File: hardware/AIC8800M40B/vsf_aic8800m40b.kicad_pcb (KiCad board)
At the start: 4 copper layers, 36.8 x 57.2 mm, 86 parts, among them J1 USB_A, J2 USB_C_Receptacle_USB2.0, J3 USB_C_Receptacle_USB2.0, J4 Micro_SD_Card_Det1, J6 Conn_Coaxial, J7 Conn_Coaxial, J8 Conn_02x15_Odd_Even, Q1 S9013, SW1 SW_Push, SW2 SW_Push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

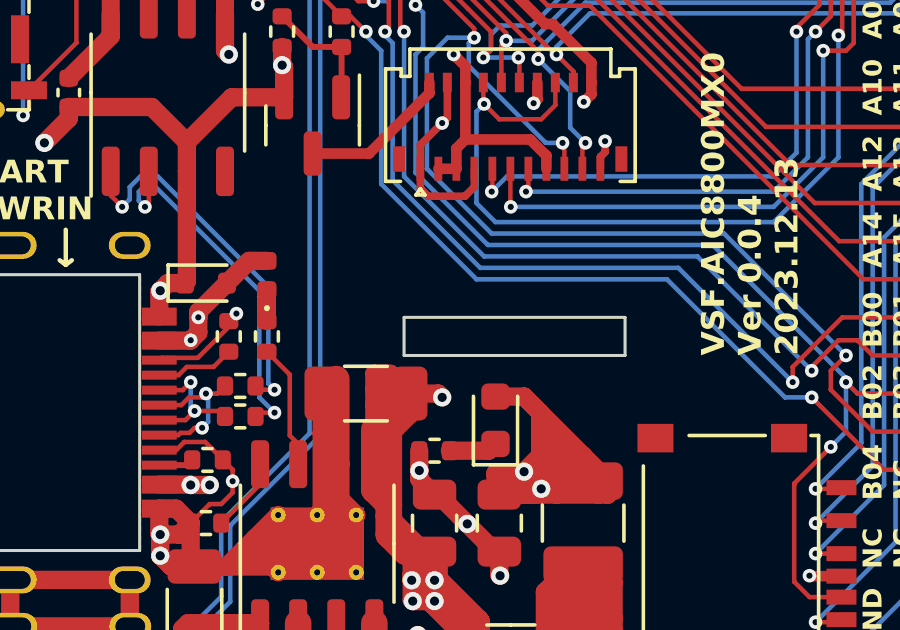
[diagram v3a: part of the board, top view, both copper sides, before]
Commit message: [hardware/aic8800m40b] update LED footprint to 0603
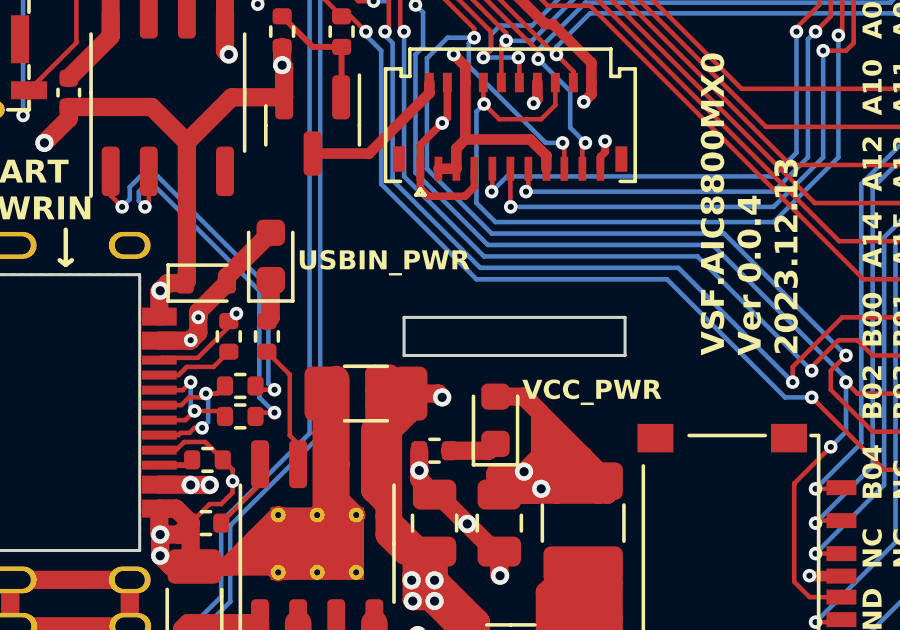
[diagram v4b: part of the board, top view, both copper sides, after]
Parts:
- D2: footprint LED_SMD:LED_0402_1005Metric -> LED_SMD:LED_0603_1608Metric
- moved D2 0.65 mm to (213.5, 124.3)
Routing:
- net /USB5V_IN: track 61.6 -> 62.2 mm
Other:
- board text added: "USBIN_PWR"
- board text added: "VCC_PWR"
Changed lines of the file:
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@@
     )
   )
-  (footprint "LED_SMD:LED_0402_1005Metric" (layer "F.Cu")
-    (at 213.36 124.968 90)
-    (descr "LED SMD 0402 (1005 Metric), square (rectangular) end terminal, IPC_7351 nominal, (Body size source: http://www.tortai-tech.com/upload/download/2011102023233369053.pdf), generated with kicad-footprint-generator")
+  (footprint "LED_SMD:LED_0603_1608Metric" (layer "F.Cu")
+    (at 213.487 124.333 90)
+    (descr "LED SMD 0603 (1608 Metric), square (rectangular) end terminal, IPC_7351 nominal, (Body size source: http://www.tortai-tech.com/upload/download/2011102023233369053.pdf), generated with kicad-footprint-generator")
     (tags "LED")
     (property "Sheetfile" "vsf_aic8800m40b.kicad_sch")
@@
     (property "ki_keywords" "LED diode")
     (attr smd)
-    (fp_text reference "D2" (at 1.524 0 180) (layer "F.SilkS") hide
-        (effects (font (size 0.762 0.762) (thickness 0.1524) bold))
+    (fp_text reference "D2" (at 0 -1.43 90) (layer "F.SilkS") hide
+        (effects (font (size 1 1) (thickness 0.15)))
     )
-    (fp_text value "LED, RED" (at 0 1.17 90) (layer "F.Fab")
+    (fp_text value "LED, RED" (at 0 1.43 90) (layer "F.Fab")
         (effects (font (size 1 1) (thickness 0.15)))
     )
     (fp_text user "${REFERENCE}" (at 0 0 90) (layer "F.Fab")
-        (effects (font (size 0.25 0.25) (thickness 0.04)))
+        (effects (font (size 0.4 0.4) (thickness 0.06)))
     )
-    (fp_circle (center -1.09 0) (end -1.04 0)
-      (stroke (width 0.1) (type solid)) (fill none) (layer "F.SilkS"))
-    (fp_line (start -0.93 -0.47) (end 0.93 -0.47)
+    (fp_line (start -1.485 -0.735) (end -1.485 0.735)
+      (stroke (width 0.12) (type solid)) (layer "F.SilkS"))
+    (fp_line (start -1.485 0.735) (end 0.8 0.735)
+      (stroke (width 0.12) (type solid)) (layer "F.SilkS"))
+    (fp_line (start 0.8 -0.735) (end -1.485 -0.735)
+      (stroke (width 0.12) (type solid)) (layer "F.SilkS"))
+    (fp_line (start -1.48 -0.73) (end 1.48 -0.73)
       (stroke (width 0.05) (type solid)) (layer "F.CrtYd"))
-    (fp_line (start -0.93 0.47) (end -0.93 -0.47)
+    (fp_line (start -1.48 0.73) (end -1.48 -0.73)
       (stroke (width 0.05) (type solid)) (layer "F.CrtYd"))
-    (fp_line (start 0.93 -0.47) (end 0.93 0.47)
+    (fp_line (start 1.48 -0.73) (end 1.48 0.73)
       (stroke (width 0.05) (type solid)) (layer "F.CrtYd"))
-    (fp_line (start 0.93 0.47) (end -0.93 0.47)
+    (fp_line (start 1.48 0.73) (end -1.48 0.73)
       (stroke (width 0.05) (type solid)) (layer "F.CrtYd"))
-    (fp_line (start -0.5 -0.25) (end 0.5 -0.25)
-      (stroke (width 0.1) (type solid)) (layer "F.Fab"))
-    (fp_line (start -0.5 0.25) (end -0.5 -0.25)
+    (fp_line (start -0.8 -0.1) (end -0.8 0.4)
       (stroke (width 0.1) (type solid)) (layer "F.Fab"))
-    (fp_line (start -0.4 0.25) (end -0.4 -0.25)
+    (fp_line (start -0.8 0.4) (end 0.8 0.4)
       (stroke (width 0.1) (type solid)) (layer "F.Fab"))
-    (fp_line (start -0.3 0.25) (end -0.3 -0.25)
+    (fp_line (start -0.5 -0.4) (end -0.8 -0.1)
       (stroke (width 0.1) (type solid)) (layer "F.Fab"))
-    (fp_line (start 0.5 -0.25) (end 0.5 0.25)
+    (fp_line (start 0.8 -0.4) (end -0.5 -0.4)
       (stroke (width 0.1) (type solid)) (layer "F.Fab"))
-    (fp_line (start 0.5 0.25) (end -0.5 0.25)
+    (fp_line (start 0.8 0.4) (end 0.8 -0.4)
       (stroke (width 0.1) (type solid)) (layer "F.Fab"))
-    (pad "1" smd roundrect (at -0.485 0 90) (size 0.59 0.64) (layers "F.Cu" "F.Paste" "F.Mask") (roundrect_rratio 0.25)
+    (pad "1" smd roundrect (at -0.7875 0 90) (size 0.875 0.95) (layers "F.Cu" "F.Paste" "F.Mask") (roundrect_rratio 0.25)
       (net 25 "Net-(D2-K)") (pinfunction "K") (pintype "passive"))
-    (pad "2" smd roundrect (at 0.485 0 90) (size 0.59 0.64) (layers "F.Cu" "F.Paste" "F.Mask") (roundrect_rratio 0.25)
+    (pad "2" smd roundrect (at 0.7875 0 90) (size 0.875 0.95) (layers "F.Cu" "F.Paste" "F.Mask") (roundrect_rratio 0.25)
       (net 20 "/USB5V_IN") (pinfunction "A") (pintype "passive"))
-    (model "${KICAD6_3DMODEL_DIR}/LED_SMD.3dshapes/LED_0402_1005Metric.wrl"
+    (model "${KICAD6_3DMODEL_DIR}/LED_SMD.3dshapes/LED_0603_1608Metric.wrl"
       (offset (xyz 0 0 0))
       (scale (xyz 1 1 1))
@@
     (effects (font (size 0.762 0.762) (thickness 0.1524) bold) (justify left bottom))
   )
+  (gr_text "VCC_PWR" (at 221.869 129.159) (layer "F.SilkS")
+    (effects (font (size 0.635 0.635) (thickness 0.1524) bold) (justify left bottom))
+  )
   (gr_text "B04\nNC" (at 234.95 132.461 90) (layer "F.SilkS")
     (effects (font (size 0.635 0.635) (thickness 0.1524) bold) (justify left bottom))
@@
     (effects (font (size 0.635 0.635) (thickness 0.1524) bold) (justify left bottom))
   )
+  (gr_text "USBIN_PWR" (at 214.376 124.841) (layer "F.SilkS")
+    (effects (font (size 0.635 0.635) (thickness 0.1524) bold) (justify left bottom))
+  )
   (gr_text "5V0\nPWR" (at 234.95 142.621 90) (layer "F.SilkS")
     (effects (font (size 0.635 0.635) (thickness 0.1524) bold) (justify left bottom))
@@
   (segment (start 213.1314 137.0076) (end 212.344 137.795) (width 0.6096) (layer "F.Cu") (net 20))
   (segment (start 212.344 136.5588) (end 212.0072 136.5588) (width 0.6096) (layer "F.Cu") (net 20))
+  (segment (start 212.028 125.222) (end 212.028 125.0045) (width 0.6096) (layer "F.Cu") (net 20))
   (segment (start 210.82 127.127) (end 211.074 126.873) (width 0.6096) (layer "F.Cu") (net 20))
   (segment (start 210.947 136.8128) (end 211.201 136.5588) (width 0.6096) (layer "F.Cu") (net 20))
@@
   (segment (start 211.074 126.176) (end 212.028 125.222) (width 0.6096) (layer "F.Cu") (net 20))
   (segment (start 210.807 131.94) (end 210.82 131.953) (width 0.6096) (layer "F.Cu") (net 20))
-  (segment (start 212.767 124.483) (end 213.36 124.483) (width 0.6096) (layer "F.Cu") (net 20))
   (segment (start 210.53616 137.20816) (end 210.947 137.619) (width 0.6096) (layer "F.Cu") (net 20))
+  (segment (start 212.028 125.0045) (end 213.487 123.5455) (width 0.6096) (layer "F.Cu") (net 20))
   (segment (start 210.5784 144.64) (end 211.074 145.1356) (width 0.6096) (layer "F.Cu") (net 20))
   (segment (start 210.947 137.619) (end 211.2838 137.619) (width 0.6096) (layer "F.Cu") (net 20))
@@
   (segment (start 213.1314 136.5588) (end 212.9452 136.5588) (width 0.6096) (layer "F.Cu") (net 20))
   (segment (start 211.074 145.288) (end 211.074 145.994703) (width 0.6096) (layer "F.Cu") (net 20))
-  (segment (start 212.028 125.222) (end 212.767 124.483) (width 0.6096) (layer "F.Cu") (net 20))
   (segment (start 213.1314 136.5588) (end 212.344 136.5588) (width 0.6096) (layer "F.Cu") (net 20))
   (segment (start 211.963 116.247) (end 211.963 117.475) (width 0.6096) (layer "F.Cu") (net 20))
@@
   (segment (start 222.345 140.587) (end 222.347 140.589) (width 0.6096) (layer "F.Cu") (net 24))
   (segment (start 221.234 140.587) (end 221.234 140.0095) (width 0.6096) (layer "F.Cu") (net 24))
-  (segment (start 213.36 125.453) (end 213.36 126.49) (width 0.6096) (layer "F.Cu") (net 25))
+  (segment (start 213.487 126.363) (end 213.36 126.49) (width 0.6096) (layer "F.Cu") (net 25))
+  (segment (start 213.487 125.1205) (end 213.487 126.363) (width 0.6096) (layer "F.Cu") (net 25))
   (segment (start 219.458 130.81) (end 220.7515 130.81) (width 0.6096) (layer "F.Cu") (net 26))
   (segment (start 220.7515 130.81) (end 220.98 130.5815) (width 0.6096) (layer "F.Cu") (net 26))

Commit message: [hardware/aic8800m40b] leave J2 open
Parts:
- JP1: value Jumper_3_Bridged12 -> Jumper_3_Open; footprint Jumper:SolderJumper-3_P1.3mm_Bridged12_RoundedPad1.0x1.5mm_NumberLabels -> Jumper:SolderJumper-3_P1.3mm_Open_RoundedPad1.0x1.5mm_NumberLabels
- R25: value 10k -> 4.7k
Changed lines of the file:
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@@
         (effects (font (size 0.762 0.762) (thickness 0.1524) bold))
     )
-    (fp_text value "10k" (at 0 1.17) (layer "F.Fab")
+    (fp_text value "4.7k" (at 0 1.17) (layer "F.Fab")
         (effects (font (size 1 1) (thickness 0.15)))
     )
@@
     )
   )
-  (footprint "Jumper:SolderJumper-3_P1.3mm_Bridged12_RoundedPad1.0x1.5mm_NumberLabels" (layer "B.Cu")
+  (footprint "Jumper:SolderJumper-3_P1.3mm_Open_RoundedPad1.0x1.5mm_NumberLabels" (layer "B.Cu")
     (at 213.868 138.811 180)
-    (descr "SMD Solder 3-pad Jumper, 1x1.5mm rounded Pads, 0.3mm gap, pads 1-2 bridged with 1 copper strip, labeled with numbers")
-    (tags "net tie solder jumper bridged")
+    (descr "SMD Solder 3-pad Jumper, 1x1.5mm rounded Pads, 0.3mm gap, open, labeled with numbers")
+    (tags "solder jumper open")
     (property "Sheetfile" "vsf_aic8800m40b.kicad_sch")
     (property "Sheetname" "")
-    (property "ki_description" "Jumper, 3-pole, pins 1+2 closed/bridged")
+    (property "ki_description" "Jumper, 3-pole, both open")
     (property "ki_keywords" "Jumper SPDT")
     (attr exclude_from_pos_files)
-    (net_tie_pad_groups "1, 2, 3")
-    (fp_text reference "JP1" (at -1.1176 -1.6256) (layer "B.SilkS") hide
-        (effects (font (size 0.762 0.762) (thickness 0.1524) bold) (justify mirror))
-    )
-    (fp_text value "Jumper_3_Bridged12" (at 0 -1.9) (layer "B.Fab")
+    (fp_text reference "JP1" (at 0 1.8) (layer "B.SilkS") hide
         (effects (font (size 1 1) (thickness 0.15)) (justify mirror))
     )
-    (fp_text user "1" (at -2.6 0) (layer "B.SilkS")
+    (fp_text value "Jumper_3_Open" (at 0 -1.9) (layer "B.Fab")
         (effects (font (size 1 1) (thickness 0.15)) (justify mirror))
     )
@@
         (effects (font (size 1 1) (thickness 0.15)) (justify mirror))
     )
-    (fp_poly
-      (pts
-        (xy -0.9 0.3)
-        (xy -0.4 0.3)
-        (xy -0.4 -0.3)
-        (xy -0.9 -0.3)
-      )
-      (stroke (width 0) (type solid)) (fill solid) (layer "B.Cu"))
+    (fp_text user "1" (at -2.6 0) (layer "B.SilkS")
+        (effects (font (size 1 1) (thickness 0.15)) (justify mirror))
+    )
     (fp_line (start -2.05 -0.3) (end -2.05 0.3)
       (stroke (width 0.12) (type solid)) (layer "B.SilkS"))
@@
       (options (clearance outline) (anchor rect))
       (primitives
+        (gr_circle (center 0 -0.25) (end 0.5 -0.25) (width 0) (fill yes))
+        (gr_circle (center 0 0.25) (end 0.5 0.25) (width 0) (fill yes))
         (gr_poly
           (pts
@@
           )
           (width 0) (fill yes))
-        (gr_circle (center 0 -0.25) (end 0.5 -0.25) (width 0) (fill yes))
-        (gr_circle (center 0 0.25) (end 0.5 0.25) (width 0) (fill yes))
       ))
     (pad "2" smd rect (at 0 0 180) (size 1 1.5) (layers "B.Cu" "B.Mask")

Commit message: [hardware/aic8800m40b] update
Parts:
- added JP2: Jumper_2_Open, VSF:SolderJumper-2_P0.8mm_Open_Pad0.6x0.8mm, F.Cu at (213.2, 139.0)
- JP1: value Jumper_3_Open -> Jumper_2_Open; footprint Jumper:SolderJumper-3_P1.3mm_Open_RoundedPad1.0x1.5mm_NumberLabels -> VSF:SolderJumper-2_P0.8mm_Open_Pad0.6x0.8mm; moved to F.Cu
- R8, R9: value 22 -> 0
- moved JP1 12.1 mm to (216.5, 127.0), turned to 0 degrees
- moved R6 0.23 mm to (212.0, 139.6)
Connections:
- C25 pad 1: /USB5V_IN -> Net-(JP2-B)
- JP1 pad 1: /VBAT -> /USB5V_IN
- JP1 pad 2: Net-(JP1-C) -> /USB5V_OUT
- SW1 pad 1: Net-(JP1-C) -> /VBAT
- U3 pad 1: /USB5V_IN -> Net-(JP2-B)
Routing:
- net Net-(JP1-C): track 30.4 -> 0.00 mm, vias 1 -> 0
- net /VBAT: track 43.0 -> 70.1 mm, vias 2 -> 3
- net Net-(JP2-B): track 0.00 -> 21.1 mm
- net /USB5V_IN: track 62.2 -> 79.2 mm, vias 10 -> 12
- net /USB5V_OUT: track 91.9 -> 100.4 mm, vias 7 -> 8
- net GND: track 347.6 -> 342.0 mm, vias 208 -> 207
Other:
- board text added: "BAT_PWR"
- board text added: "USBIN_LED"
- board text added: "USB_PWR"
- board text added: "VCC_LED"
- board text added: "VSF.AIC8800MX0 Ver 0.0.5 2024.01.12"
- board text removed: "USB"
- board text removed: "USBIN_PWR"
- board text removed: "VCC_PWR"
- board text removed: "VSF.AIC8800MX0 Ver 0.0.4 2023.12.13"

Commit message: [hardware/aic8800m40] minor tweak
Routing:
- net /USB5V_IN: track 79.2 -> 83.9 mm, vias 12 -> 14
